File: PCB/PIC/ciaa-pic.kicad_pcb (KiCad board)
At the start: 4 copper layers, 138.6 x 86.2 mm, 492 parts, among them IC1 PS2805-4, IC2 PS2805-4, J1 TB_1X3, J10 TB_1X3, J11 TB_1X2, J12 TB_1X3, J13 TB_1X3, J14 TB_1X2, J15 TB_1X3, J16 TB_1X3, J17 TB_1X2, J18 TB_1X2, J19 TB_1X2, J2 TB_1X3, J3 DB9, J4 TB_1X3, J5 RJ45-TRANSFO, J6 ZX62-AB-5PA, J7 ZX62-AB-5PA, J8 TB_1X3, J9 TB_1X3, K1 G5V-2-DC5, K2 G5V-2-DC5, K3 G5V-2-DC5, K4 G5V-2-DC5, P13 I2C, P14 SPI, P2 CONN_6X2, P3 CONN_6, P4 CONN_6, P5 CONN_13X2, P6 CONN_5X2, Q1 PBSS5240XF, Q11 NDS7002A, Q12 NDS7002A, Q14 BC817-40, Q2 FQT13N06L, Q3 FQT13N06L, Q4 FQT13N06L, Q5 FQT13N06L, Q6 NDS7002A, Q7 NDS7002A, SW1 SW_PUSH_4, U1 LAN_8740, U10 MIC2025-2YM, U11 MCP6024, U12 24AA1025, U13 24AA025E48, U14 TXB0108, U15 TPS2051B, U16 PIC32MZ2048EC, U17 FT2232H, U18 LM358, U19 93C46, U2 SI502, U20 SST26VF064BA, U21 MCP6022, U22 ASDMB-24.000MHZ-LC-T, U23 MCP1416, U24 23A1024, U25 TC25L5I32K7680, U26 MCP9700, U27 MCP1416, U28 MCP1416, U29 MCP1416, U3 LM2596-5.0, U4 NCP1117ST33T3G, U5 MAX3072, U6 ST3232E, U7 MCP2551, U8 PESD1CAN, U9 PRTR5V0U2X, X1 12MHz

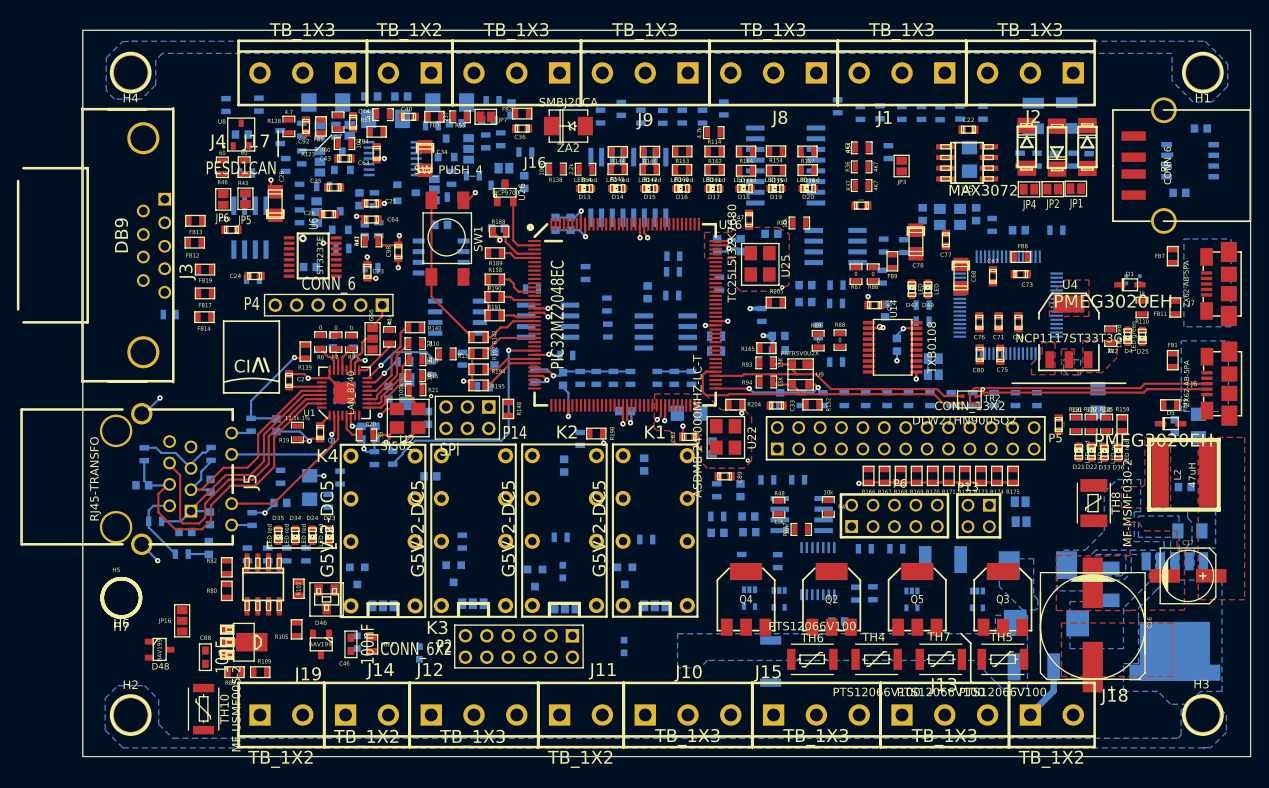
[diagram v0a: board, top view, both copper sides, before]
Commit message: Correcciones al esquematico segun rev01
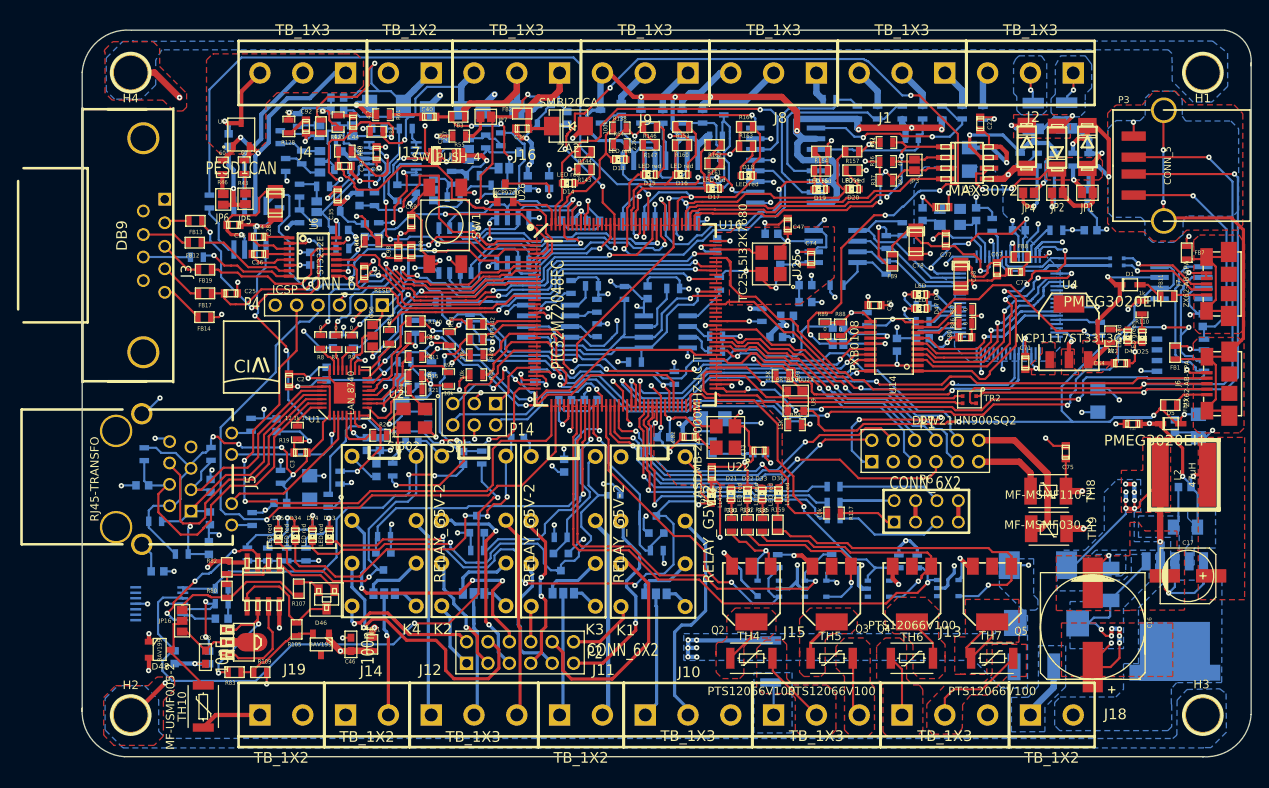
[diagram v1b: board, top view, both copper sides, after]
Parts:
- removed GS1, GS2: GS2, GS2
- removed H5, H6, H7: 4mm, 1pin
- removed P13: I2C, PIN_ARRAY_2X2
- removed P5: CONN_13X2, pin_array_13x2
- removed R151, R152: 1k, SM0603
- removed R166, R167, R168, R169, R170, R171, R172, R173, R174, R175, R176, R177, R178, R179, R180, R181, R182, R183, R184, R185, R186, R187: 10k, SM0603
- removed R188, R189, R190, R191, R192, R193, R194, R195, R196, R197, R198, R199, R200, R201, R202, R203, R204, R205, R206, R207: 10K, SM0603
- removed R42, R45: 1K5, SM0603_Resistor
- added P1: CONN_6X2, PIN_ARRAY_6X2, F.Cu at (115.3, 63.7)
- C69, C99, D27, TH9: moved to F.Cu
- C76, R114, R139, R158, R165: moved to B.Cu
- K1, K2, K3, K4: value G5V-2-DC5 -> RELAY_G5V-2
- P3: value CONN_6 -> CONN_5
- P6: value CONN_5X2 -> CONN_4X2; footprint PIN_ARRAY_5x2 -> pin_array_4x2
- Q1: footprint -SOT89-321 -> -SOT89
- U23, U27, U28, U29: footprint sot323-5 -> SOT23-5
- U7: value MCP2551 -> VP231
- moved C64 90.5 mm to (138.4, 53.3), turned to 180 degrees
- moved U21 78.3 mm to (24.3, 81.8), turned to 270 degrees
- moved R150 77.3 mm to (31.8, 80.0), turned to 180 degrees
- moved R141 75.3 mm to (31.8, 81.8), turned to 180 degrees
- moved C97 73.2 mm to (31.8, 83.6)
- moved C95 66.1 mm to (26.2, 88.1), turned to 270 degrees
- moved C96 65.8 mm to (30.3, 88.2), turned to 270 degrees
- moved R158 60.3 mm to (114.3, 76.8), turned to 90 degrees
- moved U10 52.8 mm to (145.7, 43.7)
- moved C69 50.4 mm to (54.2, 36.4), turned to 90 degrees
- moved R92 45.6 mm to (58.7, 55.1), turned to 90 degrees
- moved R49 45.5 mm to (62.0, 52.2), turned to 0 degrees
- moved R131 42.6 mm to (92.3, 72.4)
- moved R159 42.6 mm to (97.7, 72.4)
- moved R135 42.6 mm to (95.9, 72.4)
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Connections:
- C28 pad 2: +5V -> +3.3V
- C29 pad 2: +5V -> +3.3V
- D23 pad 2: N-00000401 -> N-00000355
- D24 pad 2: N-00000399 -> N-00000367
- D27 pad 1: N-00000401 -> N-00000355
- D28 pad 1: N-00000399 -> N-00000367
- D30 pad 1: N-00000363 -> N-00000371
- D31 pad 1: N-00000368 (its old number) -> N-00000370
- D34 pad 2: N-00000363 -> N-00000371
- D35 pad 2: N-00000368 (its old number) -> N-00000370
- K1 pad 1: /Salidas Digitales/NO1B -> +5V
- K1 pad 11: (no net) -> /Salidas Digitales/NC1A
- K1 pad 13: (no net) -> /Salidas Digitales/C1A
- K1 pad 16: /Salidas Digitales/NO1A -> N-00000355
- K1 pad 4: (no net) -> /Salidas Digitales/C1B
- K1 pad 6: (no net) -> /Salidas Digitales/NC1B
- K1 pad 8: +5V -> /Salidas Digitales/NO1B
- K1 pad 9: N-00000401 -> /Salidas Digitales/NO1A
- K2 pad 1: /Salidas Digitales/NO2B -> +5V
- K2 pad 11: (no net) -> /Salidas Digitales/NC3A
- K2 pad 13: (no net) -> /Salidas Digitales/C3A
- K2 pad 16: /Salidas Digitales/NO2A -> N-00000371
- K2 pad 4: (no net) -> /Salidas Digitales/C3B
- K2 pad 6: (no net) -> /Salidas Digitales/NC3B
- K2 pad 8: +5V -> /Salidas Digitales/NO3B
- K2 pad 9: N-00000399 -> /Salidas Digitales/NO3A
- K3 pad 1: /Salidas Digitales/NO3B -> +5V
- K3 pad 11: (no net) -> /Salidas Digitales/NC2A
- K3 pad 13: (no net) -> /Salidas Digitales/C2A
- K3 pad 16: /Salidas Digitales/NO3A -> N-00000367
- K3 pad 4: (no net) -> /Salidas Digitales/C2B
- K3 pad 6: (no net) -> /Salidas Digitales/NC2B
- K3 pad 8: +5V -> /Salidas Digitales/NO2B
- K3 pad 9: N-00000363 -> /Salidas Digitales/NO2A
- K4 pad 1: /Salidas Digitales/NO4B -> +5V
- K4 pad 11: (no net) -> /Salidas Digitales/NC4A
- K4 pad 13: (no net) -> /Salidas Digitales/C4A
- K4 pad 16: /Salidas Digitales/NO4A -> N-00000370
- K4 pad 4: (no net) -> /Salidas Digitales/C4B
- K4 pad 6: (no net) -> /Salidas Digitales/NC4B
- K4 pad 8: +5V -> /Salidas Digitales/NO4B
- K4 pad 9: N-00000368 (its old number) -> /Salidas Digitales/NO4A
- P2 pad 1: /Salidas Digitales/C1B -> /Salidas Digitales/NO3B
- P2 pad 10: /Salidas Digitales/NC3B -> /Salidas Digitales/NC1B
- P2 pad 11: /Salidas Digitales/NO2B -> /Salidas Digitales/C1B
- P2 pad 12: /Salidas Digitales/C3B -> /Salidas Digitales/NO1B
- P2 pad 3: /Salidas Digitales/NC1B -> /Salidas Digitales/NC3B
- P2 pad 5: /Salidas Digitales/NO1B -> /Salidas Digitales/C3B
- P2 pad 8: /Salidas Digitales/NO3B -> /Salidas Digitales/NO2B
- Q11 pad D: N-00000363 -> N-00000371
- Q12 pad D: N-00000368 (its old number) -> N-00000370
- Q6 pad D: N-00000401 -> N-00000355
- Q7 pad D: N-00000399 -> N-00000367
- U16 pad 1: /CPU/RS485_DIR -> /CPU/AIN2
- U16 pad 10: /CPU/GPIO10 -> /CPU/RESET_ETH
- U16 pad 100: /CPU/NC_100 -> (no net)
- U16 pad 103: /CPU/NC_103 -> (no net)
- U16 pad 109: /CPU/SPI_SCK -> (no net)
- U16 pad 11: /CPU/GPIO11 -> /CPU/RS232_RXD
- U16 pad 110: /CPU/RS232_RTS -> /CPU/RS485_DIR
- U16 pad 111: /CPU/GPIO20 -> /CPU/RS485_RXD
- U16 pad 112: /CPU/GPIO19 -> /CPU/RS485_TXD
- U16 pad 113: /CPU/GPIO18 -> (no net)
- U16 pad 12: /CPU/GPIO09 -> (no net)
- U16 pad 125: /CPU/GPIO17 -> /CPU/DIN3
- U16 pad 126: /CPU/GPIO16 -> /CPU/DIN2
- U16 pad 127: /CPU/GPIO15 -> (no net)
- U16 pad 128: /CPU/GPIO14 -> (no net)
- U16 pad 13: /CPU/DOUT7 -> (no net)
- U16 pad 131: /CPU/DOUT0 -> (no net)
- U16 pad 132: /CPU/DOUT1 -> (no net)
- U16 pad 133: /CPU/DOUT2 -> (no net)
- U16 pad 134: /CPU/DOUT3 -> (no net)
- U16 pad 135: /CPU/GPIO_SPI_CS -> (no net)
- U16 pad 138: /CPU/RESET_ETH -> (no net)
- U16 pad 142: /CPU/GPIO13 -> /CPU/DIN0
- U16 pad 143: /CPU/GPIO8 -> /CPU/DIN1
- U16 pad 144: /CPU/GPIO7 -> /CPU/AD_TEMP
- U16 pad 15: /CPU/NC_15 -> (no net)
- U16 pad 16: /CPU/RS485_TXD -> (no net)
- U16 pad 19: /CPU/NC_19 -> (no net)
- U16 pad 2: /CPU/AD_TEMP -> /CPU/RS232_RTS
- U16 pad 24: /CPU/NC_24 -> (no net)
- U16 pad 26: /CPU/AIN1 -> (no net)
- U16 pad 28: /CPU/NC_28 -> (no net)
- U16 pad 29: /CPU/NC_29 -> (no net)
- U16 pad 3: /CPU/RS232_CTS -> /CPU/AIN0
- U16 pad 30: /CPU/NC_30 -> (no net)
- U16 pad 34: /CPU/RS232_RXD -> /CPU/SPI_SCK
- U16 pad 35: /CPU/RS485_RXD -> /CPU/GPIO_SPI_CS
- U16 pad 36: /CPU/AIN0 -> /CPU/CAN_TD
- U16 pad 39: /CPU/Vref- -> (no net)
- U16 pad 4: /CPU/NC_4 -> /CPU/AIN1
- U16 pad 40: /CPU/Vref+ -> (no net)
- U16 pad 42: GNDA -> GND
- U16 pad 43: /CPU/AIN3 -> /CPU/DOUT7
- U16 pad 44: /CPU/AIN2 -> /CPU/DOUT5
- U16 pad 45: /CPU/GPIO2 -> /CPU/DOUT2
- U16 pad 46: /CPU/NC_46 -> /CPU/DOUT1
- U16 pad 47: /CPU/NC_47 -> /CPU/DOUT0
- U16 pad 48: /CPU/NC_48 -> /CPU/DOUT3
- U16 pad 5: /CPU/NC_5 -> /CPU/AIN3
- U16 pad 50: /CPU/NC_50 -> /CPU/DOUT4
- U16 pad 51: /CPU/NC_51 -> /CPU/GPIO13
- U16 pad 52: /CPU/NC_52 -> /CPU/GPIO2
- U16 pad 6: /GPIO/AN0 -> /CPU/RS232_CTS
- U16 pad 62: /CPU/NC_62 -> /GPIO/AN0
- U16 pad 67: /CPU/NC_67 -> (no net)
- U16 pad 69: /CPU/CAN_TD -> (no net)
- U16 pad 72: /CPU/NC_72 -> (no net)
- U16 pad 79: /CPU/DOUT5 -> (no net)
- U16 pad 82: /CPU/DIN0 -> /CPU/GPIO8
- U16 pad 83: /CPU/DIN1 -> /CPU/GPIO7
- U16 pad 86: /GPIO/GPIO6 -> (no net)
- U16 pad 9: /CPU/GPIO1 -> (no net)
- U16 pad 90: /CPU/RPF4_SDA5 -> (no net)
- U16 pad 91: /CPU/RPF5_SCL5 -> (no net)
- U16 pad 92: /CPU/GPIO21 -> (no net)
- U16 pad 93: /CPU/DIN2 -> /CPU/GPIO15
- U16 pad 94: /CPU/DIN3 -> (no net)
- U16 pad 97: /CPU/DOUT4 -> (no net)
- U16 pad 98: /CPU/NC_98 -> (no net)
- U7 pad 3: +5V -> +3.3V
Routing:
- net GND: track 119.8 -> 490.0 mm, vias 32 -> 114
- net +3.3V: track 58.3 -> 261.1 mm, vias 16 -> 65
- net /Memorias NV/SPIFI_CLK: track 0.00 -> 137.7 mm, vias 0 -> 8
- net GNDA: track 4.34 -> 132.6 mm, vias 2 -> 28
- net +5V: track 0.00 -> 128.0 mm, vias 0 -> 18
- net /USB OTG/USB0_PWR_FAULT: track 0.00 -> 118.0 mm, vias 0 -> 5
- net /USB OTG/USB0_PPWR: track 0.00 -> 115.8 mm, vias 0 -> 3
- net /Entradas Digitales/COM: track 0.00 -> 110.2 mm, vias 0 -> 7
- net /CPU/USB_VBUS: track 13.9 -> 98.9 mm, vias 2 -> 5
- net /CPU/CAN_RD: track 0.00 -> 82.3 mm, vias 0 -> 1
- net /CPU/PGED2: track 0.00 -> 78.9 mm, vias 0 -> 1
- net /CPU/RESET: track 21.4 -> 95.4 mm, vias 0 -> 2
- net N-00000417: track 0.00 -> 72.8 mm, vias 0 -> 2
- net /CPU/PGEC2: track 0.00 -> 71.7 mm, vias 0 -> 2
- net N-00000355: track 0.00 -> 71.0 mm, vias 0 -> 4
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- added copper zone on B.Cu, net /USB OTG/GND_SH
- added copper zone on F.Cu, net /USB OTG/GND_SH
- added copper zone on F.Cu, net GNDA
- added copper zone on F.Cu, net N-00000168
- added copper zone on F.Cu, net N-00000211
- added copper zone on F.Cu, net N-00000214
- added copper zone on B.Cu, net N-00000225
- added copper zone on B.Cu, net N-00000226
- added copper zone on B.Cu, net N-00000239
- added copper zone on B.Cu, net N-00000240
- added copper zone on F.Cu, net N-00000240
- added copper zone on B.Cu, net N-00000241
- added copper zone on F.Cu, net N-00000241
- added copper zone on B.Cu, net N-00000356
- added copper zone on F.Cu, net N-00000373
- added copper zone on F.Cu, net N-00000374
- added copper zone on F.Cu, net N-00000375
- added copper zone on F.Cu, net N-00000376
- added copper zone on F.Cu, net N-00000377
- added copper zone on F.Cu, net N-00000378
- added copper zone on F.Cu, net N-00000379
- added copper zone on F.Cu, net N-00000390
- removed copper zone on B.Cu, net +3.3V
- removed copper zone on B.Cu, net N-00000168 (its old number)
- removed copper zone on B.Cu, net N-00000246
- removed copper zone on F.Cu, net N-00000246
- removed copper zone on B.Cu, net N-00000254
- removed copper zone on F.Cu, net N-00000254
- removed copper zone on B.Cu, net N-00000286
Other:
- board size 138.6 x 86.2 mm -> 138.8 x 86.3 mm
- board text added: "CIAA Microchip v1.0 8/2/2016 www.proyecto-ciaa.com.ar"
- board text added: "ICSP"
- board text added: "RESET"

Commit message: cambio en plano de masa eth - CIAA-PIC
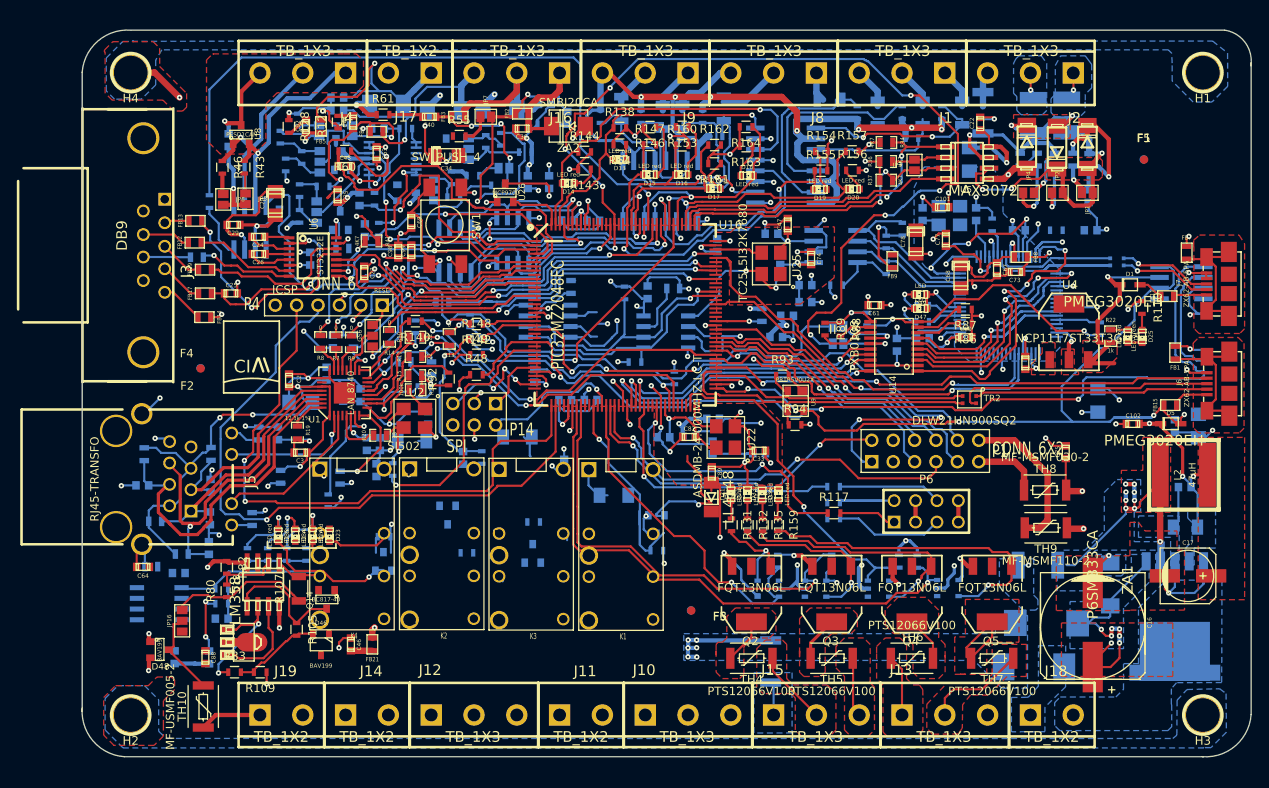
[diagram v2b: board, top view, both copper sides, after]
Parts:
- removed C65: 100nF, c_0603
- removed GS10, GS7, GS8, GS9: GS3, GS3
- removed P2: CONN_6X2, PIN_ARRAY_6X2
- removed P3: CONN_5, USB-A-Receptacle-FCI_87583
- removed R26, R27, R28, R29, R30: 0, SM0603_Resistor
- removed U15: TPS2051B, so-8
- added F1: FIDUCIAL, Fiducials:Fiducial_1mm_Dia_2.54mm_Outer_CopperTop, F.Cu at (141.2, 29.1)
- added F2: FIDUCIAL, Fiducials:Fiducial_1mm_Dia_2.54mm_Outer_CopperTop, F.Cu at (29.2, 53.9)
- added F3: FIDUCIAL, Fiducials:Fiducial_1mm_Dia_2.54mm_Outer_CopperTop, F.Cu at (87.5, 82.6)
- added F4: FIDUCIAL, Fiducials:Fiducial_1mm_Dia_2.54mm_Outer_CopperBottom, F.Cu at (29.2, 53.8)
- added F5: FIDUCIAL, Fiducials:Fiducial_1mm_Dia_2.54mm_Outer_CopperBottom, F.Cu at (141.2, 29.1)
- added F6: FIDUCIAL, Fiducials:Fiducial_1mm_Dia_2.54mm_Outer_CopperBottom, F.Cu at (87.5, 82.6)
- C1, C18, C31, C34, C78: footprint c_1206_tantalio_1 -> footprints:c_1206_tantalio
- C10, C100, C101, C102, C103, C104, C11, C12, C13, C14, C15, C19, C2, C20, C22, C23, C24, C25, C26, C27, C29, C3, C30, C32, C33, C35, C36, C37, C38, C39, C4, C40, C41, C42, C43, C44, C45, C47, C48, C49, C50, C51, C52, C53, C54, C55, C56, C57, C58, C59, C6, C61, C62, C63, C67, C69, C7, C70, C71, C72, C73, C74, C75, C76, C77, C8, C80, C82, C83, C84, C85, C86, C87, C89, C9, C90, C91, C92, C93, C94, C95, C96, C97, C98, C99: footprint c_0603 -> footprints:c_0603
- C16: footprint c_elec_13.7x13x13.5 -> footprints:c_elec_13.7x13x13.5
- C17: footprint c_elec_6.3x7.7 -> footprints:c_elec_6.3x7.7
- C21, C28: value 10uF / 6V3 -> 10uF/6V3; footprint c_1206_tantalio -> footprints:c_1206_tantalio
- C46, C88: footprint SMC0603 -> footprints:c_0603
- C5: footprint c_1206_tantalio_1 -> footprints:c_0603
- C60: footprint c_1206_tantalio -> footprints:c_0603
- C64: value 100nF -> 100nf; footprint c_0603 -> footprints:c_0603
- C66: value 10nF -> 100nF; footprint c_0603 -> footprints:c_0603
- C68: footprint c_1206_tantalio -> footprints:c_1206_tantalio
- C79, C81: value 27p -> 12p; footprint c_0603 -> footprints:c_0603
- D1, D5: footprint SOD323 -> footprints:SOD323
- D10, D11, D12, D9, U26: footprint SOT23 -> footprints:SOT23
- D13, D14, D15, D16, D17, D18, D19, D20, D21, D22, D23, D24, D25, D33, D34, D35, D36, D4, D47, D49: footprint LED-0603 -> footprints:LED-0603
- D2: footprint DO-214AB(SMC) -> Diodes_SMD:DO-214AB
- D27, D28, D30, D31: footprint LED-0603 -> footprints:1n4148
- D3: footprint Diode-SMC_Standard_RevA_26July2010 -> footprints:DO-214AB(SMC)
- D46: footprint SOT23-DIODE -> footprints:SOT23-DIODE
- D48: footprint SOT23-DIODE -> footprints:SOT23
- D6, D7, D8: footprint DO214AA-1-2 -> footprints:DO214AA-1-2
- FB1, FB11, FB12, FB13, FB14, FB15, FB17, FB18, FB19, FB2, FB21, FB3, FB4, FB5, FB7, FB8, FB9, L1: footprint SM0603 -> footprints:SM0603
- FB20, FB6, R31: footprint SM0603 -> footprints:SM0603_Resistor
- GS3, GS4, JP1, JP11, JP13, JP2, JP3, JP4, JP5, JP6, JP7, JP9: footprint GS2 -> footprints:GS2
- GS6, JP10, JP12, JP14, JP16, JP8: footprint GS3 -> footprints:GS3
- H1, H2, H3, H4: footprint 1pin -> footprints:1pin
- IC1, IC2: footprint -SOP16 -> footprints:-SOP16
- J1, J10, J12, J13, J15, J16, J2, J4, J8, J9: footprint bornier3 -> footprints:bornier3
- J11, J14, J17, J18, J19: footprint bornier2 -> footprints:bornier2
- J3: footprint K22X-E9P-NJ -> footprints:K22X-E9P-NJ
- J5: footprint RJ45_TRANSFO -> footprints:RJ45_TRANSFO
- J6, J7: footprint USB_microAB_ZX62-AB&B-5PA-11 -> footprints:USB_microAB_ZX62-AB&B-5PA-11
- K1, K2, K3, K4: value RELAY_G5V-2 -> RELAY_TE_1461353-2; footprint G5V-2 -> footprints:1461353-2
- L2: footprint Inductor_10x9.8mm -> footprints:Inductor_10x9.8mm
- P1: footprint PIN_ARRAY_6X2 -> footprints:PIN_ARRAY_6X2
- P14: footprint PIN_ARRAY_3X2 -> footprints:PIN_ARRAY_3X2
- P4: footprint PIN_ARRAY_6X1 -> footprints:PIN_ARRAY_6X1
- P6: footprint pin_array_4x2 -> footprints:pin_array_4x2
- PS1, PS2: footprint SM1210 -> footprints:MF-MSMF
- Q1: footprint -SOT89 -> footprints:-SOT89
- Q11, Q12, Q6, Q7: footprint SOT23GDS -> footprints:SOT23
- Q14: footprint -SOT23 -> footprints:SOT23
- Q2, Q3, Q4, Q5: footprint SOT223_Opendous -> footprints:SOT223
- R1, R10, R11, R12, R13, R14, R15, R16, R17, R18, R19, R2, R20, R21, R22, R23, R24, R3, R33, R34, R36, R37, R38, R4, R41, R5, R6, R7, R8, R9: footprint SM0603_Resistor -> footprints:SM0603_Resistor
- R100, R101, R102, R103, R104, R106, R108, R110, R111, R112, R114, R115, R116, R117, R118, R119, R120, R121, R122, R123, R124, R125, R126, R127, R128, R129, R130, R131, R132, R133, R134, R135, R136, R137, R138, R43, R44, R46, R47, R48, R49, R50, R51, R52, R53, R54, R55, R56, R57, R58, R59, R60, R61, R62, R63, R64, R73, R74, R75, R76, R77, R78, R79, R84, R85, R86, R87, R88, R89, R90, R91, R92, R93, R94, R95, R97, R98, R99: footprint SM0603_Resistor -> Resistors_SMD:R_0603
- R105, R109, R113, R139, R140, R141, R142, R143, R144, R146, R147, R148, R149, R150, R153, R154, R155, R156, R157, R158, R159, R160, R161, R162, R163, R164, R165, R80, R81, R82, R83: footprint SM0603 -> Resistors_SMD:R_0603
- R107: footprint SM0603 -> Resistors_SMD:R_1206
- R145: value 220 -> 270; footprint SM0603 -> Resistors_SMD:R_0603
- R25: value 0 -> 1M; footprint SM0603_Resistor -> footprints:SM0603_Resistor
- R32, R39: value 680 -> 390; footprint SM0603_Resistor -> footprints:SM0603_Resistor
- R35: value 120 -> 220; footprint SM0603_Resistor -> footprints:SM0603_Resistor
- R40: footprint SM0603_Resistor -> Resistors_SMD:R_2010
- R65, R66, R67, R68, R69, R70, R71, R72: footprint SM0603_Resistor -> Resistors_SMD:R_1206
- R96: value 220 -> 270; footprint SM0603_Resistor -> Resistors_SMD:R_0603
- SW1: footprint PUSH_SWITCH -> footprints:PUSH_SWITCH
- TH1: footprint MF-SM030 -> footprints:2-SMD-MF-SM030
- TH10, TH3, TH4, TH5, TH6, TH7: footprint MF-USMF -> footprints:MF-USMF
- TH8, TH9: footprint MF-MSMF -> footprints:MF-USMF
- TR1, TR2: footprint SRF2012 -> footprints:SRF2012
- U1: footprint QFN32_Opendous -> footprints:QFN32_Opendous
- U10, U18, U19, U5, U7: footprint -SOIC8 -> footprints:-SOIC8
- U11: footprint TSSOP14 -> footprints:TSSOP14
- U12, U13: footprint -SOIC8 -> footprints:SO8-sst
- U14: footprint tssop-20 -> footprints:tssop-20
- U16: footprint LQFP144-M05 -> footprints:LQFP144-M05
- U17: footprint LQFP64-M05 -> footprints:LQFP64-M05
- U2, U22, U25: footprint 4SMD -> footprints:4SMD
- U20: footprint SO8 -> footprints:SO8-sst
- U21: footprint TSSOP14 -> footprints:SO8-sst
- U23, U27, U28, U29: footprint SOT23-5 -> footprints:SOT23-5
- U24: footprint SO8E -> footprints:-SOIC8
- U3: footprint D2PACK5-LM2596 -> footprints:TO263-6--D2PACK5-LM2596
- U4: footprint SOT223 -> footprints:SOT223
- U6: footprint TSSOP16 -> footprints:TSSOP16
- U8: footprint SOT23-3 -> footprints:SOT23
- U9: footprint sot143B -> footprints:sot143B
- X1: value 12MHz -> FA-238V; footprint FA238V-XTAL -> footprints:4SMD
- ZA1: footprint DO-214AC(SMA) -> footprints:DO214AA-1-2
- ZA14: footprint SOD123F -> footprints:SOD123F
- ZA2, ZA3, ZA4, ZA5: footprint DO-214AA(SMB) -> footprints:DO-214AA(SMB)
- moved C64 118.5 mm to (22.4, 77.4)
- moved R25 62.0 mm to (23.4, 77.4), turned to 0 degrees
- moved C10 14.8 mm to (46.2, 57.0), turned to 90 degrees
- moved C1 10.2 mm to (41.1, 57.9), turned to 0 degrees
- moved C5 4.93 mm to (48.2, 57.0), turned to 90 degrees
- moved R112 3.69 mm to (68.8, 72.1)
- moved Q11 3.63 mm to (58.6, 71.3)
- moved Q7 3.50 mm to (68.7, 75.8)
- moved C9 2.53 mm to (26.6, 78.2), turned to 180 degrees
- moved R18 1.39 mm to (36.1, 61.6)
- moved R115 1.25 mm to (60.9, 75.8)
- moved C4 0.98 mm to (38.4, 61.6)
- moved TH8 0.39 mm to (129.5, 68.3), turned to 0 degrees
- moved TH9 0.38 mm to (129.6, 72.8), turned to 180 degrees
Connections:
- net /CPU/EECLK renamed /JTAG/EECLK
- net /CPU/EECS renamed /JTAG/EECS
- net /CPU/EEDATA renamed /JTAG/EEDATA
- net /CPU/FT_OE renamed /JTAG/FT_OE
- net /CPU/FT_RST renamed /JTAG/FT_RST
- net /CPU/FT_TCK renamed /JTAG/FT_TCK
- net /CPU/FT_TDI renamed /JTAG/FT_TDI
- net /CPU/FT_TDO renamed /JTAG/FT_TDO
- net /CPU/FT_TMS renamed /JTAG/FT_TMS
- net /CPU/FT_TRST renamed /JTAG/FT_TRST
- net /CPU/RST renamed Net-(GS3-Pad1)
- net /CPU/TRST renamed Net-(GS4-Pad1)
- net /CPU/USB_DEBUG_VBUS renamed /JTAG/USB_DEBUG_VBUS
- net /CPU/USB_JTAG_1.8V renamed /JTAG/USB_JTAG_1.8V
- net /CPU/USB_JTAG_DM renamed /JTAG/USB_JTAG_DM
- net /CPU/USB_JTAG_DP renamed /JTAG/USB_JTAG_DP
- net /Entradas Digitales/IN0 renamed Net-(J1-Pad1)
- net /Entradas Digitales/IN1 renamed Net-(J1-Pad2)
- net /Entradas Digitales/IN2 renamed Net-(J1-Pad3)
- net /Entradas Digitales/IN3 renamed Net-(J8-Pad1)
- net /Entradas Digitales/IN4 renamed Net-(J8-Pad2)
- net /Entradas Digitales/IN5 renamed Net-(J8-Pad3)
- net /Entradas Digitales/IN6 renamed Net-(J9-Pad1)
- net /Entradas Digitales/IN7 renamed Net-(J9-Pad2)
- net /USB OTG/D+ renamed Net-(J6-Pad3)
- net /USB OTG/D- renamed Net-(J6-Pad2)
- net /USB OTG/GND_SH renamed Net-(FB1-Pad2)
- net N-00000246 renamed /Ethernet/TXD0
- net N-00000247 renamed /Ethernet/TXD1
- net N-00000248 renamed /Ethernet/TXEN
- net N-00000250 renamed /Ethernet/MDC
- net N-00000253 renamed /Ethernet/RXER
- net N-00000257 renamed /Ethernet/XTAL1
- net N-00000259 renamed /Ethernet/RXD2
- net N-00000261 renamed /Ethernet/RXD0
- net N-00000262 renamed /Ethernet/RXCLK
- net N-00000263 renamed /Ethernet/RXD3
- net N-00000267 renamed /Ethernet/CRS_DV
- net N-00000269 renamed /Ethernet/MDIO
- net N-00000270 renamed /Ethernet/RXD1
- C1 pad 1: N-00000271 -> /Ethernet/+Filter
- C10 pad 1: N-00000271 -> /Ethernet/+Filter
- C2 pad 1: N-00000271 -> /Ethernet/+Filter
- C3 pad 1: N-00000271 -> /Ethernet/+Filter
- C5 pad 1: N-00000271 -> /Ethernet/+Filter
- C6 pad 1: N-00000271 -> /Ethernet/+Filter
- C64 pad 1: +5V -> Net-(C64-Pad1)
- C79 pad 2: /CPU/FT_XTIN -> Net-(C79-Pad2)
- C81 pad 2: /CPU/FT_XTOUT -> Net-(C81-Pad2)
- D23 pad 2: N-00000355 -> Net-(D23-Pad2)
- D24 pad 2: N-00000367 -> Net-(D24-Pad2)
- D27 pad 1: N-00000355 -> Net-(D23-Pad2)
- D28 pad 1: N-00000367 -> Net-(D24-Pad2)
- D30 pad 1: N-00000371 -> Net-(D30-Pad1)
- D31 pad 1: N-00000370 -> Net-(D31-Pad1)
- D34 pad 2: N-00000371 -> Net-(D30-Pad1)
- D35 pad 2: N-00000370 -> Net-(D31-Pad1)
- J10 pad 1: N-00000358 -> /Salidas Digitales/NC1A
- J11 pad 1: N-00000362 -> /Salidas Digitales/NC2A
- J12 pad 2: N-00000393 -> /Salidas Digitales/NC3A
- J13 pad 3: (no net) -> GND
- J14 pad 2: N-00000402 -> /Salidas Digitales/NC4A
- J5 pad 13: GND -> Net-(C64-Pad1)
- J5 pad 2: N-00000271 -> /Ethernet/+Filter
- J5 pad 5: N-00000271 -> /Ethernet/+Filter
- J5 pad 8: GND -> Net-(C64-Pad1)
- K1 pad 11: /Salidas Digitales/NC1A -> (no net)
- K1 pad 13: /Salidas Digitales/C1A -> (no net)
- K1 pad 16: N-00000355 -> Net-(D30-Pad1)
- K1 pad 4: /Salidas Digitales/C1B -> /Salidas Digitales/NC3A
- K1 pad 6: /Salidas Digitales/NC1B -> (no net)
- K1 pad 8: /Salidas Digitales/NO1B -> /Salidas Digitales/C3A
- K1 pad 9: /Salidas Digitales/NO1A -> (no net)
- K2 pad 11: /Salidas Digitales/NC3A -> (no net)
- K2 pad 13: /Salidas Digitales/C3A -> (no net)
- K2 pad 16: N-00000371 -> Net-(D23-Pad2)
- K2 pad 4: /Salidas Digitales/C3B -> /Salidas Digitales/NC1A
- K2 pad 6: /Salidas Digitales/NC3B -> (no net)
- K2 pad 8: /Salidas Digitales/NO3B -> /Salidas Digitales/C1A
- K2 pad 9: /Salidas Digitales/NO3A -> (no net)
- K3 pad 11: /Salidas Digitales/NC2A -> (no net)
- K3 pad 13: /Salidas Digitales/C2A -> (no net)
- K3 pad 16: N-00000367 -> Net-(D31-Pad1)
- K3 pad 4: /Salidas Digitales/C2B -> /Salidas Digitales/NC4A
- K3 pad 6: /Salidas Digitales/NC2B -> (no net)
- K3 pad 8: /Salidas Digitales/NO2B -> /Salidas Digitales/C4A
- K3 pad 9: /Salidas Digitales/NO2A -> (no net)
- K4 pad 11: /Salidas Digitales/NC4A -> (no net)
- K4 pad 13: /Salidas Digitales/C4A -> (no net)
- K4 pad 16: N-00000370 -> Net-(D24-Pad2)
- K4 pad 4: /Salidas Digitales/C4B -> /Salidas Digitales/NC2A
- K4 pad 6: /Salidas Digitales/NC4B -> (no net)
- K4 pad 8: /Salidas Digitales/NO4B -> /Salidas Digitales/C2A
- K4 pad 9: /Salidas Digitales/NO4A -> (no net)
- L1 pad 1: +3.3V -> /Ethernet/+Filter
- L1 pad 2: N-00000271 -> +3.3V
- R25 pad 1: GND -> Net-(C64-Pad1)
- R25 pad 2: N-00000230 -> GND
- R3 pad 1: N-00000271 -> /Ethernet/+Filter
- R4 pad 1: N-00000271 -> /Ethernet/+Filter
- R5 pad 1: N-00000271 -> /Ethernet/+Filter
- R6 pad 1: N-00000271 -> /Ethernet/+Filter
- R98 pad 1: +3.3V -> Net-(R98-Pad1)
- R98 pad 2: N-0000097 -> +3.3V
- U1 pad 1: N-00000271 -> /Ethernet/+Filter
- U1 pad 27: N-00000271 -> /Ethernet/+Filter
- U12 pad 1: N-00000230 -> GND
- U12 pad 2: N-00000231 -> GND
- U12 pad 3: N-00000237 -> +3.3V
- U13 pad 1: N-00000232 -> +3.3V
- U13 pad 2: N-00000233 -> GND
- U13 pad 3: N-00000234 -> GND
- U16 pad 23: /USB OTG/USB0_PWR_FAULT -> /CPU/SPI_SCK
- U16 pad 34: /CPU/SPI_SCK -> /USB OTG/USB0_PWR_FAULT
- U17 pad 14: N-0000097 -> Net-(R98-Pad1)
- U17 pad 2: /CPU/FT_XTIN -> Net-(C79-Pad2)
- U17 pad 3: /CPU/FT_XTOUT -> Net-(C81-Pad2)
- U21 pad 4: +3.3V -> GNDA
- U21 pad 8: (no net) -> +3.3V
- X1 pad 1: /CPU/FT_XTOUT -> Net-(C79-Pad2)
- X1 pad 2: /CPU/FT_XTIN -> GND
- X1 pad 3: (no net) -> Net-(C81-Pad2)
- X1 pad 4: (no net) -> GND
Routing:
- net /USB OTG/USB0_PWR_FAULT: track 118.0 -> 13.9 mm, vias 5 -> 0
- net N-00000271: track 79.1 -> 0.00 mm, vias 5 -> 0
- net Net-(C95-Pad2): track 72.8 -> 0.39 mm, vias 2 -> 0
- net /Ethernet/+Filter: track 0.00 -> 72.2 mm, vias 0 -> 4
- net N-00000355: track 71.0 -> 0.00 mm, vias 4 -> 0
- net /CPU/CAN_TD: track 57.3 -> 0.05 mm, vias 5 -> 0
- net N-00000367: track 54.9 -> 0.00 mm, vias 1 -> 0
- net Net-(J6-Pad2): track 75.9 -> 27.7 mm, vias 2 -> 0
- net Net-(J6-Pad3): track 77.5 -> 30.4 mm, vias 2 -> 0
- net N-00000371: track 41.8 -> 0.00 mm, vias 3 -> 0
- net /CPU/GPIO3: track 41.7 -> 0.00 mm, vias 2 -> 0
- net /CPU/DOUT3: track 41.7 -> 2.00 mm, vias 1 -> 0
- net Net-(FB1-Pad2): track 55.8 -> 17.2 mm, vias 2 -> 0
- net N-00000370: track 36.0 -> 0.00 mm, vias 1 -> 0
- net /Salidas Digitales/C4B: track 34.9 -> 0.00 mm, vias 3 -> 0
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- added copper zone on Inner2.Cu, net /CPU/USB_JTAG_1.8V
- added copper zone on F.Cu, net /USB OTG/GND_SH
- added copper zone on F.Cu, net N-00000168
- added copper zone on F.Cu, net N-00000211
- added copper zone on F.Cu, net N-00000214
- added copper zone on B.Cu, net N-00000225
- added copper zone on B.Cu, net N-00000226
- added copper zone on B.Cu, net N-00000239
- added copper zone on B.Cu, net N-00000240
- added copper zone on F.Cu, net N-00000240
- added copper zone on B.Cu, net N-00000241
- added copper zone on F.Cu, net N-00000241
- added copper zone on B.Cu, net N-00000356
- added copper zone on F.Cu, net N-00000373
- added copper zone on F.Cu, net N-00000374
- added copper zone on F.Cu, net N-00000375
- added copper zone on F.Cu, net N-00000376
- added copper zone on F.Cu, net N-00000377
- added copper zone on F.Cu, net N-00000378
- added copper zone on F.Cu, net N-00000379
- added copper zone on F.Cu, net N-00000390
- removed copper zone on Inner2.Cu, net /JTAG/USB_JTAG_1.8V
- removed copper zone on B.Cu, net Net-(C16-Pad1)
- removed copper zone on F.Cu, net Net-(C16-Pad1)
- removed copper zone on F.Cu, net Net-(C25-Pad1)
- removed copper zone on F.Cu, net Net-(C26-Pad1)
- removed copper zone on B.Cu, net Net-(D2-Pad1)
- removed copper zone on B.Cu, net Net-(D3-Pad2)
- removed copper zone on F.Cu, net Net-(D3-Pad2)
- removed copper zone on B.Cu, net Net-(FB1-Pad2)
- removed copper zone on F.Cu, net Net-(FB1-Pad2)
- removed copper zone on F.Cu, net Net-(FB7-Pad1)
- removed copper zone on F.Cu, net Net-(J13-Pad1)
- removed copper zone on F.Cu, net Net-(J13-Pad2)
- removed copper zone on B.Cu, net Net-(J15-Pad1)
- removed copper zone on F.Cu, net Net-(J15-Pad2)
- removed copper zone on F.Cu, net Net-(J15-Pad3)
- removed copper zone on B.Cu, net Net-(J2-Pad1)
- removed copper zone on B.Cu, net Net-(J2-Pad2)
- removed copper zone on F.Cu, net Net-(Q2-Pad4)
- removed copper zone on F.Cu, net Net-(Q3-Pad4)
- removed copper zone on F.Cu, net Net-(Q4-Pad4)
- removed copper zone on F.Cu, net Net-(Q5-Pad4)
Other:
- board text added: "CIAA Microchip PI32MZ v1.0 8/2/2016 www.proyecto-ciaa.com.ar"
- board text removed: "CIAA Microchip v1.0 8/2/2016 www.proyecto-ciaa.com.ar"

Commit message: correcciones pcb
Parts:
- C101: moved to B.Cu
- moved C101 5.57 mm to (118.0, 29.2), turned to 270 degrees
- moved J7 2.40 mm to (148.6, 41.4)
- moved X1 2.09 mm to (117.3, 37.0), turned to 90 degrees
- moved C79 0.96 mm to (114.9, 34.6)
- moved C81 0.92 mm to (121.6, 34.7)
- moved Q11 0.35 mm to (58.3, 71.5)
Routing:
- net /USB OTG/USB0_PWR_FAULT: track 13.9 -> 0.00 mm
- net Net-(J7-Pad3): track 11.4 -> 0.00 mm, vias 1 -> 0
- net Net-(J7-Pad2): track 11.0 -> 0.00 mm, vias 1 -> 0
- net Net-(FB7-Pad1): track 15.7 -> 6.39 mm
- net /USB OTG/USB0_PPWR: track 115.8 -> 106.7 mm
- net Net-(C79-Pad2): track 1.53 -> 10.4 mm
- net Net-(R98-Pad1): track 0.00 -> 5.91 mm
- net Net-(C77-Pad1): track 10.2 -> 15.3 mm, vias 2 -> 1
- net Net-(FB11-Pad1): track 3.97 -> 0.21 mm
- net Net-(C81-Pad2): track 4.73 -> 7.96 mm
- net +3.3V: track 262.6 -> 265.2 mm, vias 61 -> 62
- net GND: track 466.1 -> 467.9 mm, vias 100 -> 97
- net /Memorias NV/SPIFI_CLK: track 137.7 -> 139.0 mm
- net +5V: track 106.6 -> 107.7 mm, vias 15 -> 14
- net (no net): track 26.1 -> 27.1 mm
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
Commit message: correccion pcb
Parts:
- added ?: Symbol_OSHW-Logo_SilkScreen, Symbols:Symbol_OSHW-Logo_SilkScreen, F.Cu at (146.6, 29.5)
- added ?: Symbol_OSHW-Logo_SilkScreen, Symbols:Symbol_OSHW-Logo_SilkScreen, B.Cu at (147.1, 26.9)
- added REF**: Measurement_Point_Round-SMD-Pad_Small, Measurement_Points:Measurement_Point_Round-SMD-Pad_Small, F.Cu at (135.6, 65.5)
- C46, FB21: moved to B.Cu
- Q11, Q12, Q6, Q7: footprint footprints:SOT23 -> footprints:SOT23GDS
- moved J12 25.4 mm to (87.1, 95.0)
- moved J14 25.4 mm to (74.4, 95.0)
- moved J10 25.4 mm to (61.7, 95.0)
- moved J11 25.4 mm to (49.0, 95.0)
- moved D30 9.00 mm to (63.5, 70.4), turned to 180 degrees
- moved F3 5.02 mm to (84.8, 86.9)
- moved F6 5.01 mm to (84.8, 86.9)
- moved K1 4.39 mm to (87.1, 72.1)
- moved K3 4.37 mm to (76.5, 72.1)
- moved K2 4.31 mm to (65.8, 72.1)
- moved K4 4.30 mm to (55.1, 72.1)
- moved Q7 3.90 mm to (72.4, 77.0)
- moved R112 3.16 mm to (71.9, 72.6), turned to 0 degrees
- moved C94 2.43 mm to (72.1, 67.8), turned to 180 degrees
- moved R115 2.38 mm to (58.5, 75.5)
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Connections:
- J10 pad 1: /Salidas Digitales/NC1A -> /Salidas Digitales/C1A
- J10 pad 2: /Salidas Digitales/C1A -> /Salidas Digitales/NC1A
- J11 pad 1: /Salidas Digitales/NC2A -> /Salidas Digitales/C2A
- J11 pad 2: /Salidas Digitales/C2A -> /Salidas Digitales/NC2A
- J12 pad 1: /Salidas Digitales/C4A -> /Salidas Digitales/NC4A
- J12 pad 2: /Salidas Digitales/NC3A -> /Salidas Digitales/C3A
- J12 pad 3: /Salidas Digitales/C3A -> /Salidas Digitales/NC3A
- J14 pad 2: /Salidas Digitales/NC4A -> /Salidas Digitales/C4A
- J5 pad 8: Net-(C64-Pad1) -> GND
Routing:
- net /CPU/DOUT7: track 66.6 -> 3.91 mm, vias 1 -> 0
- net /CPU/DOUT5: track 53.6 -> 5.01 mm, vias 1 -> 0
- net /Salidas Digitales/NC3A: track 0.55 -> 27.5 mm
- net /Salidas Digitales/NC4A: track 2.26 -> 26.8 mm, vias 1 -> 0
- net +3.3VADC: track 23.6 -> 46.8 mm, vias 4 -> 6
- net /Salidas Digitales/NC1A: track 0.00 -> 21.8 mm
- net /Salidas Digitales/NC2A: track 1.51 -> 22.1 mm, vias 1 -> 0
- net (no net): track 27.1 -> 9.49 mm, vias 5 -> 7
- net /Salidas Digitales/C4A: track 0.48 -> 16.9 mm
- net Net-(D23-Pad2): track 15.6 -> 0.23 mm, vias 1 -> 0
- net /Salidas Digitales/C3A: track 0.55 -> 15.7 mm
- net /Salidas Digitales/C1A: track 0.78 -> 13.6 mm, vias 1 -> 0
- net /Salidas Digitales/C2A: track 0.96 -> 13.0 mm
- net Net-(C64-Pad1): track 10.6 -> 21.5 mm, vias 2 -> 0
- net Net-(D10-Pad2): track 0.06 -> 8.96 mm
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- added copper zone on F.Cu, net Net-(D6-Pad1)
- added copper zone on F.Cu, net Net-(D6-Pad2)
- removed copper zone on F.Cu, net N-00000211
- removed copper zone on F.Cu, net N-00000214
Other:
- board text added: "R.term CAN"
